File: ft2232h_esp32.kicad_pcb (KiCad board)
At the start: 4 copper layers, 60 parts, among them J1 USB_C_Receptacle_USB2.0, Q1 S8050, Q2 S8050, SW1 SW_SPDT, U1 ESP32FullConnector, U2 ESP32FullConnector, U3 USBLC6-2SC6-Power_Protection, U4 93C56-C173182, U5 FT2232HL, U6 ESP32FullConnector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

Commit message: update
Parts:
- removed C16: 2.2uf, Capacitor_SMD:C_0603_1608Metric
- removed D1: ESDLC5V0PB8, Package_DFN_QFN:UDFN-9_1.0x3.8mm_P0.5mm
- added C19: 22pf, Capacitor_SMD:C_0603_1608Metric, F.Cu at (54.6, 104.2)
- added C20: 22pf, Capacitor_SMD:C_0603_1608Metric, F.Cu at (59.0, 100.7)
- added C21: 1uf, Capacitor_SMD:C_0603_1608Metric, F.Cu at (58.6, 103.2)
- added C22: 22uf/6.3v, Capacitor_SMD:C_1206_3216Metric, F.Cu at (55.4, 94.2)
- added H5: MountingHole, MountingHole:MountingHole_2.2mm_M2, F.Cu at (43.6, 95.5)
- added H6: MountingHole, MountingHole:MountingHole_2.2mm_M2, F.Cu at (43.6, 101.4)
- added H7: MountingHole, MountingHole:MountingHole_2.2mm_M2, F.Cu at (49.6, 95.5)
- added H8: MountingHole, MountingHole:MountingHole_2.2mm_M2, F.Cu at (49.6, 101.4)
- added L1: 2.2uh, Inductor_SMD:L_01005_0402Metric, F.Cu at (62.2, 97.8)
- added R19: 100k, Resistor_SMD:R_0603_1608Metric, F.Cu at (51.0, 81.6)
- added R20: 22k, Resistor_SMD:R_0603_1608Metric, F.Cu at (55.0, 81.6)
- added R21: 10k, Resistor_SMD:R_0603_1608Metric, F.Cu at (62.6, 103.2)
- added U10: USBLC6-2SC6-Power_Protection, Package_TO_SOT_SMD:SOT-23-6, F.Cu at (109.0, 102.2)
- added U11: USBLC6-2SC6-Power_Protection, Package_TO_SOT_SMD:SOT-23-6, F.Cu at (109.0, 106.9)
- added U12: USBLC6-2SC6-Power_Protection, Package_TO_SOT_SMD:SOT-23-6, F.Cu at (113.8, 102.2)
- added U13: USBLC6-2SC6-Power_Protection, Package_TO_SOT_SMD:SOT-23-6, F.Cu at (113.8, 106.9)
- added U9: SY8089AAAC, Package_TO_SOT_SMD:TSOT-23-5, B.Cu at (114.6, 54.1)
- C17: moved to F.Cu
- C18: value 2.2uf -> 22pf; moved to F.Cu
- C7, C8: value C -> 20pf
- R18: value 10k -> 1k
- U8: value SPX1117M3-L/TR -> XC6206P332MR; footprint Package_TO_SOT_SMD:SOT-223-3_TabPin2 -> Package_TO_SOT_SMD:SOT-23; moved to F.Cu
- moved C18 74.9 mm to (54.6, 101.6), turned to 0 degrees
- moved U8 72.2 mm to (54.8, 98.1)
- moved C17 71.3 mm to (59.0, 98.2)
- moved U4 45.4 mm to (139.8, 76.1)
- moved D2 1.42 mm to (117.9, 66.5)
- moved U1 0.94 mm to (111.7, 51.0)
- moved U2 0.75 mm to (122.6, 58.3)
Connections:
- C18 pad 2: +3V3 -> 3v3OUT
- C7 pad 2: Net-(C7-Pad2) -> GND
- C8 pad 2: Net-(C8-Pad2) -> GND
- D5 pad 1: Net-(D5-Pad1) -> GND
- D5 pad 2: GND -> Net-(D5-Pad2)
- R18 pad 1: 3v3OUT -> Net-(R18-Pad1)
- R18 pad 2: Net-(D5-Pad1) -> +3V3
- SW1 pad 1: Net-(SW1-Pad1) -> Net-(R18-Pad1)
- SW1 pad 2: 3v3OUT -> Net-(D5-Pad2)
- U3 pad 1: Net-(U3-Pad1) -> USB_DP
- U3 pad 3: Net-(U3-Pad3) -> USB_DN
- U3 pad 4: Net-(U3-Pad4) -> USB_DN
- U3 pad 5: Net-(U3-Pad5) -> VBUS
- U3 pad 6: Net-(U3-Pad6) -> USB_DP
- U5 pad 2: Net-(U5-Pad2) -> Net-(C7-Pad1)
- U5 pad 3: Net-(U5-Pad3) -> Net-(C8-Pad1)
- X1 pad 1: Net-(X1-Pad1) -> Net-(C7-Pad1)
- X1 pad 2: Net-(X1-Pad2) -> GND
- X1 pad 3: Net-(X1-Pad3) -> Net-(C8-Pad1)
- X1 pad 4: Net-(X1-Pad4) -> GND

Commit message: layout
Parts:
- C10, C14, C18, C19, C2, C20, C22, C3, C7, C8, R16, R19, R20, R3, R4, X1: moved to B.Cu
- L1: footprint Inductor_SMD:L_01005_0402Metric -> Inductor_SMD:L_1008_2520Metric; moved to B.Cu
- U10, U13: footprint Package_TO_SOT_SMD:SOT-23-6 -> KisonCommon:USBLC6-2P6-SOT666
- U11, U12, U3: footprint Package_TO_SOT_SMD:SOT-23-6 -> KisonCommon:USBLC6-2P6-SOT666; moved to B.Cu
- moved C20 80.4 mm to (121.7, 50.3)
- moved C19 78.2 mm to (118.5, 59.1), turned to 90 degrees
- moved C18 77.3 mm to (120.7, 61.7), turned to 90 degrees
- moved C22 76.8 mm to (124.2, 60.0), turned to 180 degrees
- moved L1 76.6 mm to (124.3, 52.9)
- moved R19 73.5 mm to (120.7, 58.4), turned to 270 degrees
- moved R20 71.0 mm to (120.7, 54.7), turned to 90 degrees
- moved R21 68.1 mm to (115.9, 60.8), turned to 90 degrees
- moved C7 67.9 mm to (125.7, 93.8), turned to 270 degrees
- moved H5 66.1 mm to (100.0, 61.0), turned to 90 degrees
- moved H7 65.6 mm to (100.0, 53.5), turned to 90 degrees
- moved C8 65.5 mm to (123.8, 93.9), turned to 270 degrees
- moved H2 64.6 mm to (116.3, 56.3)
- moved H3 63.2 mm to (108.8, 56.3)
- moved H6 57.3 mm to (99.8, 90.0), turned to 90 degrees
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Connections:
- C21 pad 1: Net-(C21-Pad1) -> GND
- Q1 pad 3: EN -> nTRST
- U10 pad 5: +3V3 -> Net-(U10-Pad5)
- U11 pad 5: +3V3 -> Net-(U11-Pad5)
- U12 pad 5: +3V3 -> Net-(U12-Pad5)
- U13 pad 5: +3V3 -> Net-(U13-Pad5)
- U3 pad 2: Net-(U3-Pad2) -> GND
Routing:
- net GND: track 0.00 -> 321.5 mm, vias 0 -> 16
- net +3V3: track 0.00 -> 125.3 mm, vias 0 -> 8
- net TCK: track 0.00 -> 76.8 mm, vias 0 -> 2
- net VBUS: track 0.00 -> 71.9 mm, vias 0 -> 4
- net TDO: track 0.00 -> 65.0 mm, vias 0 -> 2
- net TMS: track 0.00 -> 64.9 mm, vias 0 -> 3
- net TDI: track 0.00 -> 55.0 mm, vias 0 -> 3
- net RXD: track 0.00 -> 51.5 mm, vias 0 -> 2
- net nTRST: track 0.00 -> 49.0 mm, vias 0 -> 2
- net +1V8: track 0.00 -> 45.6 mm, vias 0 -> 3
- net IO0: track 0.00 -> 43.7 mm, vias 0 -> 3
- net TXD: track 0.00 -> 43.2 mm, vias 0 -> 1
- net 3v3OUT: track 0.00 -> 32.9 mm, vias 0 -> 1
- net Net-(R12-Pad1): track 0.00 -> 29.3 mm, vias 0 -> 2
- net Net-(J1-PadS1): track 0.00 -> 25.3 mm
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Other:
- board outline added: 35 x 49.3 mm

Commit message: Fix Crystal
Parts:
- added R22: 0, Resistor_SMD:R_0603_1608Metric, B.Cu at (124.8, 67.1)
- added R23: 0, Resistor_SMD:R_0603_1608Metric, B.Cu at (122.8, 66.5)
- added R24: 0, Resistor_SMD:R_0603_1608Metric, B.Cu at (119.5, 52.3)
- C18, C20: value 22pf -> 22uf
- U1, U6, U7: footprint KisonCommon:jtag1.27-12 -> KisonCommon:jtag1.27-10
- U2: footprint Connector_Molex:Molex_CLIK-Mate_502382-1270_1x12-1MP_P1.25mm_Vertical -> Connector_Molex:Molex_CLIK-Mate_502382-1070_1x10-1MP_P1.25mm_Vertical
- X1: footprint Oscillator:Oscillator_SMD_Abracon_ASCO-4Pin_1.6x1.2mm -> Oscillator:Oscillator_SMD_Fordahl_DFAS15-4Pin_5.0x3.2mm
- moved C8 2.32 mm to (122.0, 95.3)
- moved R4 1.59 mm to (118.0, 92.9)
- moved J1 1.59 mm to (115.5, 93.0)
- moved R3 1.59 mm to (113.2, 92.9)
- moved U3 1.59 mm to (118.6, 92.4)
- moved C7 1.45 mm to (125.5, 95.3)
- moved X1 0.86 mm to (123.6, 90.5), turned to 270 degrees
- moved U2 0.81 mm to (122.5, 60.8)
- moved R20 0.06 mm to (120.7, 54.7), turned to 270 degrees
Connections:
- R20 pad 1: Net-(C19-Pad2) -> Net-(R20-Pad1)
- R20 pad 2: GND -> Net-(C19-Pad2)
- U1 pad 10: RXD -> ESPRX
- U1 pad 8: Net-(U1-Pad8) -> IO0
- U1 pad 9: TXD -> ESPTX
- U10 pad 1: TXD -> ESPTX
- U10 pad 3: RXD -> ESPRX
- U10 pad 4: RXD -> ESPRX
- U10 pad 6: TXD -> ESPTX
- U2 pad 10: RXD -> ESPRX
- U2 pad 8: Net-(U2-Pad8) -> IO0
- U2 pad 9: TXD -> ESPTX
- U4 pad 8: Net-(U4-Pad8) -> +3V3
- U5 pad 38: TXD -> 2232TX
- U5 pad 39: RXD -> 2232RX
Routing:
- net RXD: track 51.5 -> 0.00 mm, vias 2 -> 0
- net ESPRX: track 0.00 -> 43.5 mm, vias 0 -> 2
- net TXD: track 43.2 -> 0.00 mm, vias 1 -> 0
- net ESPTX: track 0.00 -> 34.8 mm, vias 0 -> 2
- net 2232TX: track 0.00 -> 22.6 mm, vias 0 -> 2
- net 2232RX: track 0.00 -> 13.8 mm
- net GND: track 321.5 -> 313.9 mm
- net VBUS: track 71.9 -> 65.7 mm, vias 4 -> 3
- net IO0: track 43.7 -> 48.2 mm
- net +1V8: track 45.6 -> 49.9 mm
- net Net-(R11-Pad1): track 7.79 -> 5.20 mm
- net Net-(C7-Pad1): track 11.6 -> 14.0 mm
- net Net-(R20-Pad1): track 0.00 -> 1.73 mm
- net 3v3OUT: track 32.9 -> 34.2 mm
- net TMS: track 64.9 -> 63.8 mm
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
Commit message: V1
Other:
- board text added: "1"
- board text added: "10"
- board text added: "JLCJLCJLCJLC"
- board text added: "KisonHe FT2232C-V1"
- board text added: "O3V3"
- board text added: "Power"
- board text added: "RX"
- board text added: "TX"

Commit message: Add SLDPRT;Fix PCB Parts interference
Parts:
- U11: moved to F.Cu
- moved U11 4.78 mm to (111.5, 51.3), turned to 270 degrees
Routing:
- net nTRST: track 49.4 -> 56.0 mm, vias 2 -> 3
- net TDI: track 55.2 -> 60.0 mm, vias 3 -> 4
- net GND: track 313.9 -> 315.2 mm, vias 16 -> 17

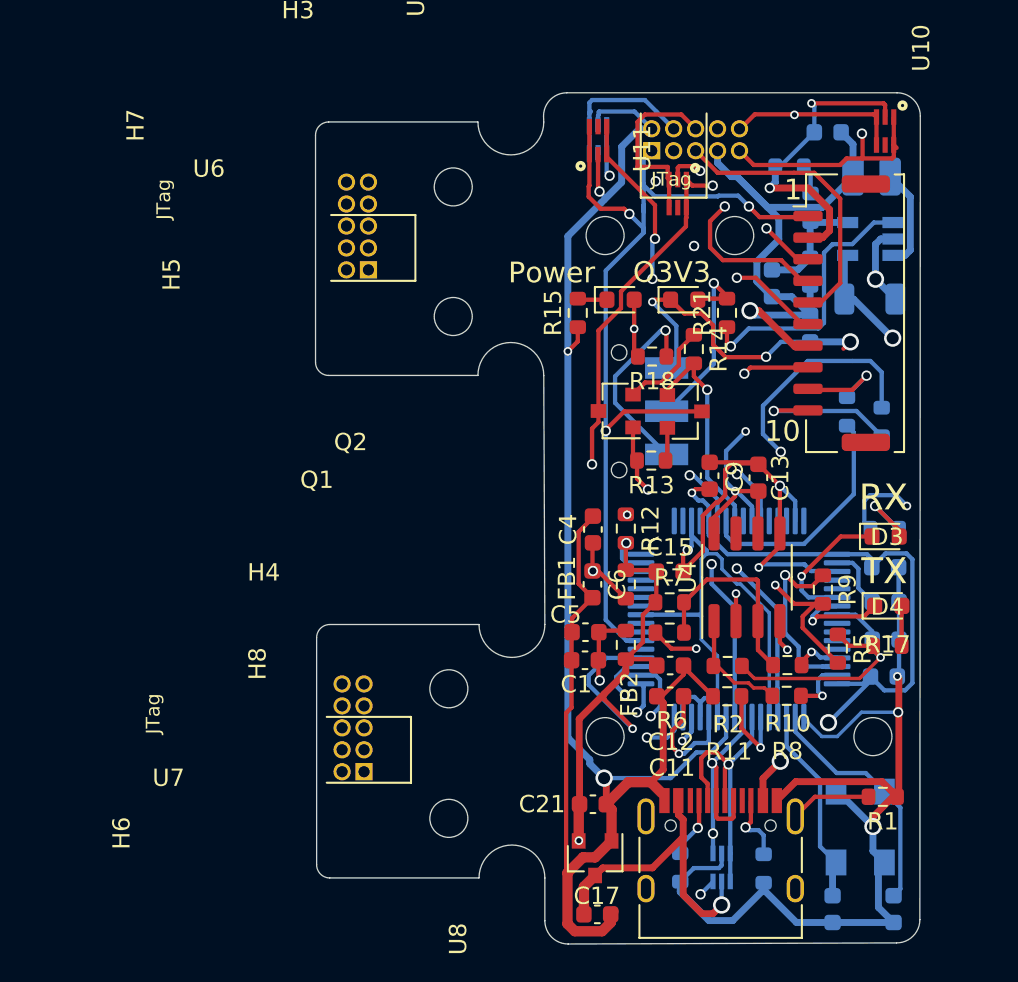
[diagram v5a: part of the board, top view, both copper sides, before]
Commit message: Detach Under Board
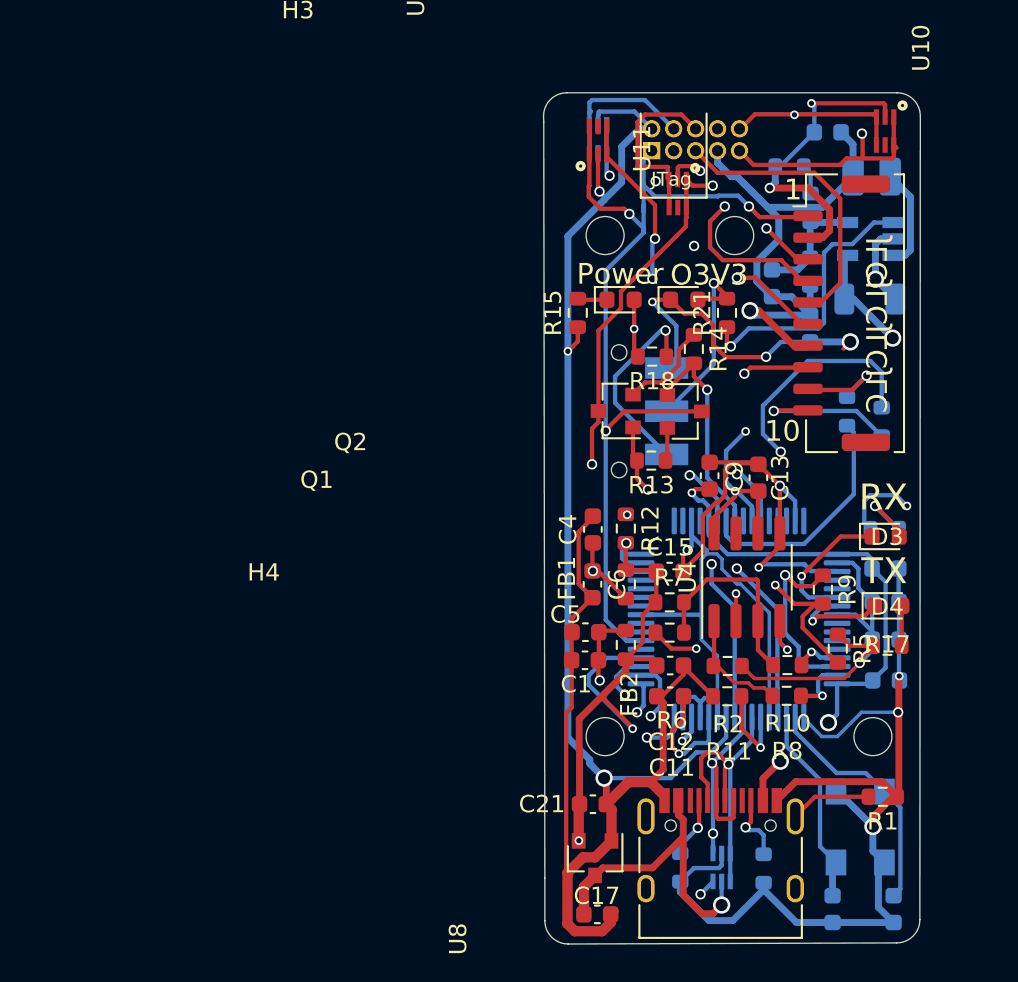
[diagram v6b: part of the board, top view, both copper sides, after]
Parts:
- removed H5, H6, H7, H8: MountingHole, MountingHole:MountingHole_2.2mm_M2
- removed U6, U7: ESP32FullConnector, KisonCommon:jtag1.27-10
- moved C10 6.55 mm to (125.1, 82.0)
- moved C3 6.25 mm to (125.1, 75.6)
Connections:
- C2 pad 1: Net-(C2-Pad1) -> +3V3
- U5 pad 50: Net-(C2-Pad1) -> +3V3
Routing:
- net +1V8: track 49.9 -> 42.9 mm
- net +3V3: track 124.7 -> 130.3 mm
- net Net-(C2-Pad1): track 3.62 -> 0.00 mm
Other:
- board size 35 x 49.3 mm -> 21.8 x 49.3 mm
- board text added: "KisonHe FT2232C-V2"
- board text removed: "KisonHe FT2232C-V1"

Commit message: V3
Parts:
- removed R22, R23: 0, Resistor_SMD:R_0603_1608Metric
- moved U10 6.22 mm to (128.1, 50.7), turned to 270 degrees
- moved SW1 1.57 mm to (108.1, 66.5)
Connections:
- U1 pad 1: nTRST -> 3v3OUT
- U1 pad 10: ESPRX -> 2232TX
- U1 pad 3: TDI -> TCK
- U1 pad 4: TCK -> TDO
- U1 pad 5: TMS -> TDI
- U1 pad 6: TDO -> TMS
- U1 pad 7: 3v3OUT -> nTRST
- U1 pad 9: ESPTX -> 2232RX
- U10 pad 1: ESPTX -> 2232RX
- U10 pad 3: ESPRX -> 2232TX
- U10 pad 4: ESPRX -> 2232TX
- U10 pad 6: ESPTX -> 2232RX
- U11 pad 1: nTRST -> TDO
- U11 pad 6: nTRST -> TDO
- U12 pad 1: TCK -> TMS
- U12 pad 3: TMS -> TCK
- U12 pad 4: TMS -> TCK
- U12 pad 6: TCK -> TMS
- U13 pad 1: IO0 -> nTRST
- U13 pad 3: TDO -> IO0
- U13 pad 4: TDO -> IO0
- U13 pad 6: IO0 -> nTRST
- U2 pad 1: nTRST -> 3v3OUT
- U2 pad 10: ESPRX -> 2232TX
- U2 pad 3: TDI -> TCK
- U2 pad 4: TCK -> TDO
- U2 pad 5: TMS -> TDI
- U2 pad 6: TDO -> TMS
- U2 pad 7: 3v3OUT -> nTRST
- U2 pad 9: ESPTX -> 2232RX
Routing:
- net ESPRX: track 43.5 -> 0.00 mm, vias 2 -> 0
- net ESPTX: track 34.8 -> 0.00 mm, vias 2 -> 0
- net 2232RX: track 13.8 -> 46.5 mm, vias 0 -> 1
- net TCK: track 77.1 -> 53.1 mm, vias 2 -> 3
- net 2232TX: track 22.6 -> 44.6 mm, vias 2 -> 3
- net TDI: track 60.0 -> 77.7 mm, vias 4 -> 3
- net IO0: track 48.2 -> 63.4 mm
- net TDO: track 65.2 -> 56.9 mm
- net nTRST: track 56.0 -> 49.9 mm, vias 3 -> 2
- net +3V3: track 130.3 -> 125.2 mm
- net GND: track 314.8 -> 319.7 mm, vias 17 -> 16
- net Net-(C1-Pad1): track 24.6 -> 22.3 mm
- net 3v3OUT: track 34.2 -> 35.7 mm
- net TMS: track 63.8 -> 65.1 mm
- net Net-(D5-Pad2): track 11.5 -> 12.5 mm
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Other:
- board text added: "KisonHe FT2232C-V3"
- board text removed: "KisonHe FT2232C-V2"
